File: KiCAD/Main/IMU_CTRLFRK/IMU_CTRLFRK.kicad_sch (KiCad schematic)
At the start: 9 parts, among them U3 BMM350, U7 ISM6HG256x

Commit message: Moved custom footprints into local KiCAD footprint library
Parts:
- U3: footprint BMM350:BGA9C40P3X3_128X128X50 -> LRI:BGA9C40P3X3_128X128X50
- U7: footprint ISM6HG256XTR:U_LGA-14L_2p5X3p0X0p83_STM -> LRI:ISM6
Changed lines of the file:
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@@
 			)
 		)
-		(property "Footprint" "BMM350:BGA9C40P3X3_128X128X50"
+		(property "Footprint" "LRI:BGA9C40P3X3_128X128X50"
 			(at 190.5 101.6 0)
 			(effects
@@
 			)
 		)
-		(property "Footprint" "ISM6HG256XTR:U_LGA-14L_2p5X3p0X0p83_STM"
+		(property "Footprint" "LRI:ISM6"
 			(at 127 101.6 0)
 			(effects

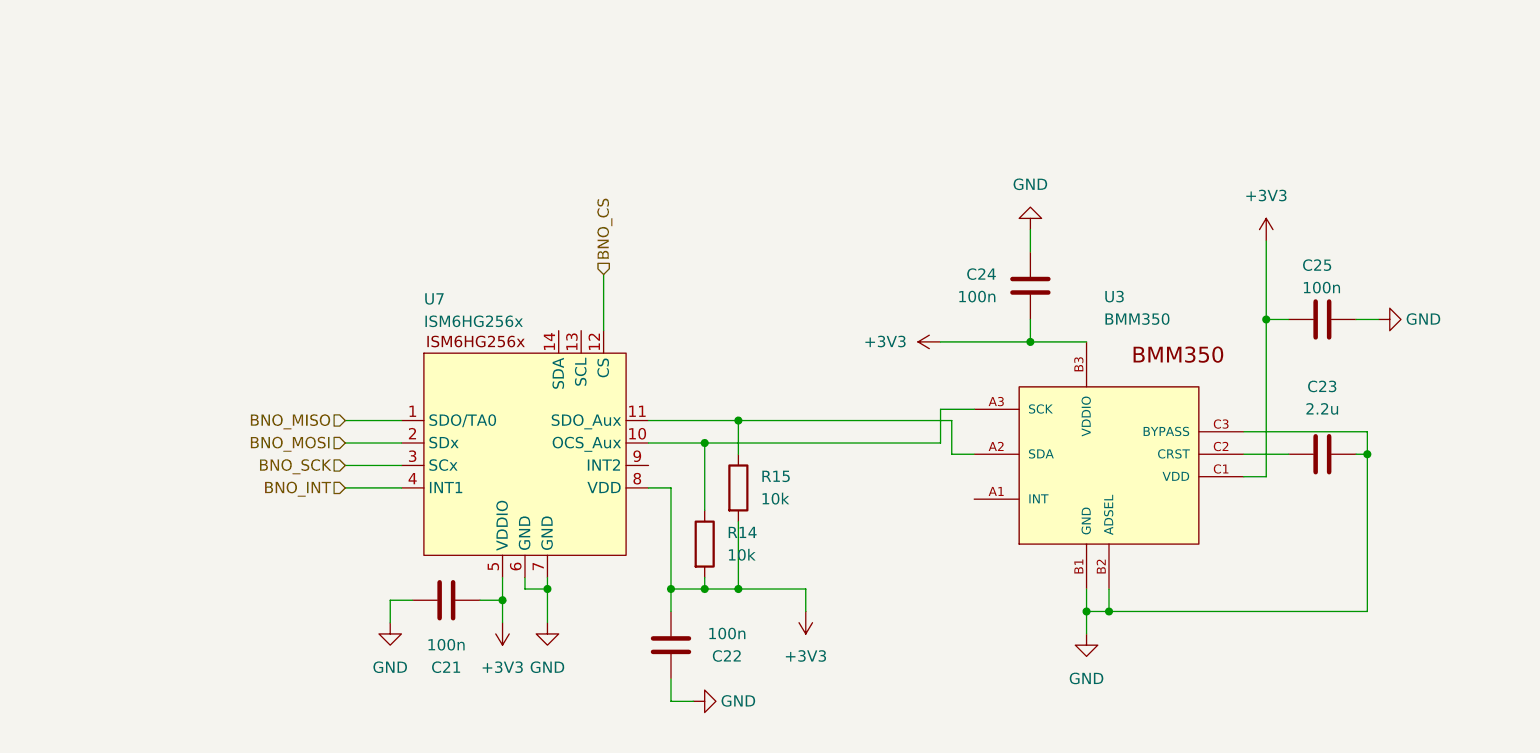
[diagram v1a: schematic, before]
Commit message: Fixed controller SCL/SDA pins
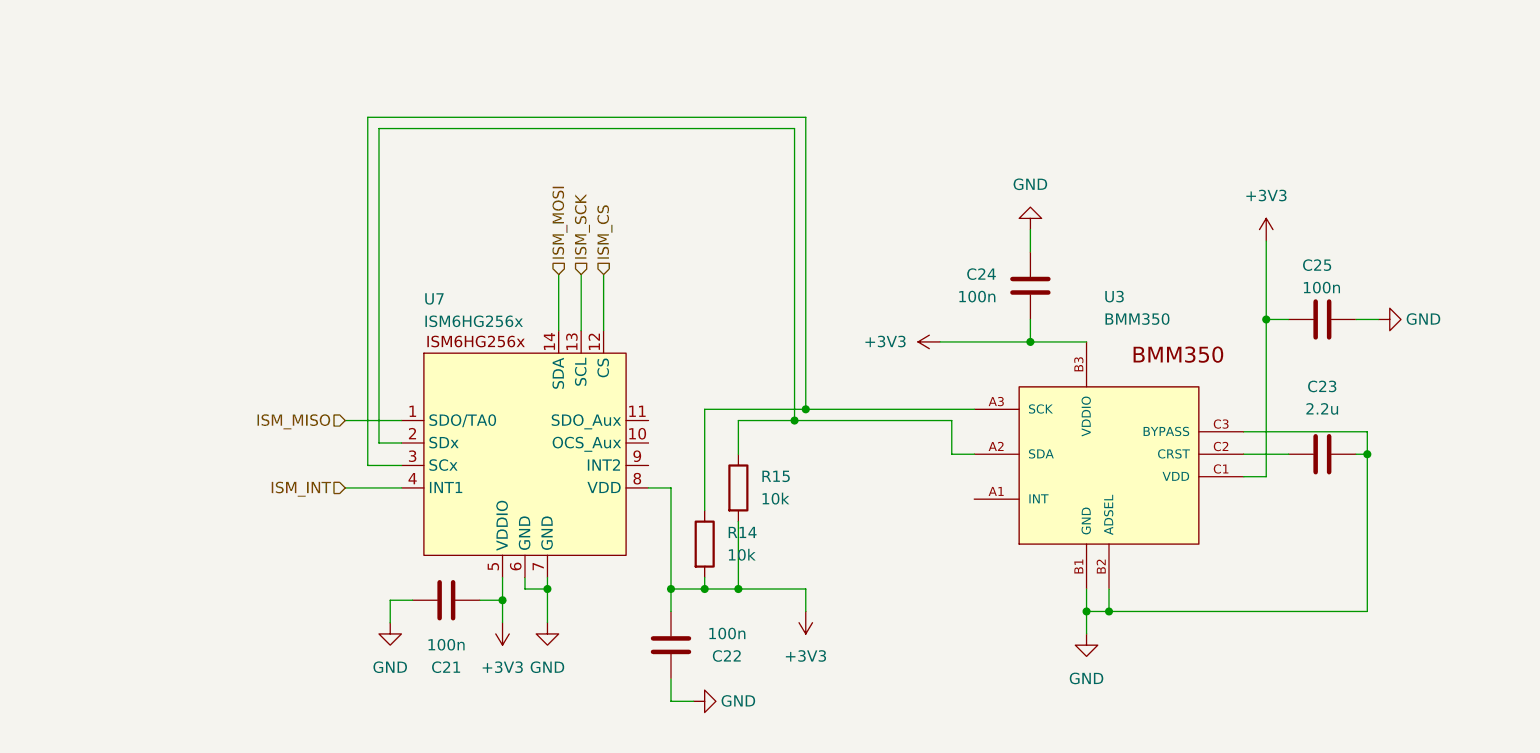
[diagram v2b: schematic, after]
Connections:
- net BNO_MOSI is gone; now on an unnamed net: U7.2 (SDx)
- net BNO_SCK is gone; now on an unnamed net: U7.3 (SCx)
- net at R15.1, U3.A2 (SDA): no longer U7.11 (SDO_Aux)
- net at R14.1, U3.A3 (SCK): no longer U7.10 (OCS_Aux)
- net ISM_SCK: now reaches U7.13 (SCL)
- net ISM_MOSI: now reaches U7.14 (SDA)
- net BNO_CS renamed ISM_CS
- net BNO_INT renamed ISM_INT
- net BNO_MISO renamed ISM_MISO
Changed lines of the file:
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@@
 	(paper "A4")
 	(junction
-		(at 147.32 100.33)
-		(diameter 0)
-		(color 0 0 0 0)
-	)
-	(junction
 		(at 147.32 116.84)
 		(diameter 0)
@@
 	)
 	(junction
+		(at 157.48 97.79)
+		(diameter 0)
+		(color 0 0 0 0)
+	)
+	(junction
 		(at 151.13 116.84)
 		(diameter 0)
@@
 	)
 	(junction
-		(at 151.13 97.79)
+		(at 158.75 96.52)
 		(diameter 0)
 		(color 0 0 0 0)
@@
 	(wire
 		(pts
-			(xy 140.97 97.79) (xy 151.13 97.79)
+			(xy 113.03 102.87) (xy 109.22 102.87)
 		)
 		(stroke
@@
 	(wire
 		(pts
+			(xy 109.22 102.87) (xy 109.22 63.5)
+		)
+		(stroke
+			(width 0)
+			(type default)
+		)
+	)
+	(wire
+		(pts
 			(xy 111.76 120.65) (xy 111.76 118.11)
 		)
@@
 	(wire
 		(pts
+			(xy 113.03 100.33) (xy 110.49 100.33)
+		)
+		(stroke
+			(width 0)
+			(type default)
+		)
+	)
+	(wire
+		(pts
 			(xy 121.92 118.11) (xy 124.46 118.11)
 		)
@@
 	(wire
 		(pts
-			(xy 173.99 96.52) (xy 173.99 100.33)
+			(xy 110.49 64.77) (xy 157.48 64.77)
+		)
+		(stroke
+			(width 0)
+			(type default)
+		)
+	)
+	(wire
+		(pts
+			(xy 133.35 81.28) (xy 133.35 87.63)
 		)
 		(stroke
@@
 	(wire
 		(pts
-			(xy 140.97 100.33) (xy 147.32 100.33)
-		)
-		(stroke
-			(width 0)
-			(type default)
-		)
-	)
-	(wire
-		(pts
 			(xy 124.46 115.57) (xy 124.46 118.11)
 		)
@@
 	(wire
 		(pts
-			(xy 173.99 96.52) (xy 177.8 96.52)
-		)
-		(stroke
-			(width 0)
-			(type default)
-		)
-	)
-	(wire
-		(pts
 			(xy 190.5 116.84) (xy 190.5 119.38)
 		)
@@
 	(wire
 		(pts
-			(xy 113.03 102.87) (xy 106.68 102.87)
-		)
-		(stroke
-			(width 0)
-			(type default)
-		)
-	)
-	(wire
-		(pts
 			(xy 143.51 116.84) (xy 143.51 105.41)
 		)
@@
 	(wire
 		(pts
+			(xy 157.48 97.79) (xy 175.26 97.79)
+		)
+		(stroke
+			(width 0)
+			(type default)
+		)
+	)
+	(wire
+		(pts
 			(xy 184.15 76.2) (xy 184.15 78.74)
 		)
@@
 	(wire
 		(pts
-			(xy 113.03 100.33) (xy 106.68 100.33)
-		)
-		(stroke
-			(width 0)
-			(type default)
-		)
-	)
-	(wire
-		(pts
-			(xy 173.99 100.33) (xy 147.32 100.33)
+			(xy 147.32 96.52) (xy 158.75 96.52)
 		)
 		(stroke
@@
 	(wire
 		(pts
+			(xy 157.48 64.77) (xy 157.48 97.79)
+		)
+		(stroke
+			(width 0)
+			(type default)
+		)
+	)
+	(wire
+		(pts
 			(xy 222.25 101.6) (xy 220.98 101.6)
 		)
@@
 	(wire
 		(pts
+			(xy 158.75 96.52) (xy 177.8 96.52)
+		)
+		(stroke
+			(width 0)
+			(type default)
+		)
+	)
+	(wire
+		(pts
 			(xy 106.68 105.41) (xy 113.03 105.41)
 		)
@@
 	(wire
 		(pts
+			(xy 109.22 63.5) (xy 158.75 63.5)
+		)
+		(stroke
+			(width 0)
+			(type default)
+		)
+	)
+	(wire
+		(pts
 			(xy 151.13 109.22) (xy 151.13 116.84)
 		)
@@
 	(wire
 		(pts
+			(xy 130.81 81.28) (xy 130.81 87.63)
+		)
+		(stroke
+			(width 0)
+			(type default)
+		)
+	)
+	(wire
+		(pts
 			(xy 208.28 101.6) (xy 213.36 101.6)
 		)
@@
 	(wire
 		(pts
-			(xy 151.13 97.79) (xy 175.26 97.79)
+			(xy 151.13 97.79) (xy 157.48 97.79)
 		)
 		(stroke
@@
 	(wire
 		(pts
-			(xy 147.32 100.33) (xy 147.32 107.95)
+			(xy 147.32 96.52) (xy 147.32 107.95)
+		)
+		(stroke
+			(width 0)
+			(type default)
+		)
+	)
+	(wire
+		(pts
+			(xy 110.49 100.33) (xy 110.49 64.77)
 		)
 		(stroke
@@
 		)
 	)
-	(hierarchical_label "BNO_SCK"
+	(wire
+		(pts
+			(xy 158.75 63.5) (xy 158.75 96.52)
+		)
+		(stroke
+			(width 0)
+			(type default)
+		)
+	)
+	(hierarchical_label "ISM_MOSI"
 		(shape input)
-		(at 106.68 102.87 180)
+		(at 130.81 81.28 90)
 		(effects
 			(font
 				(size 1.27 1.27)
 			)
-			(justify right)
-		)
-	)
-	(hierarchical_label "BNO_MISO"
+			(justify left)
+		)
+	)
+	(hierarchical_label "ISM_MISO"
 		(shape input)
 		(at 106.68 97.79 180)
@@
 		)
 	)
-	(hierarchical_label "BNO_MOSI"
+	(hierarchical_label "ISM_SCK"
 		(shape input)
-		(at 106.68 100.33 180)
+		(at 133.35 81.28 90)
 		(effects
 			(font
 				(size 1.27 1.27)
 			)
-			(justify right)
-		)
-	)
-	(hierarchical_label "BNO_CS"
+			(justify left)
+		)
+	)
+	(hierarchical_label "ISM_CS"
 		(shape input)
 		(at 135.89 81.28 90)
@@
 		)
 	)
-	(hierarchical_label "BNO_INT"
+	(hierarchical_label "ISM_INT"
 		(shape input)
 		(at 106.68 105.41 180)

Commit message: Changed BMM350 for LIS2MDL
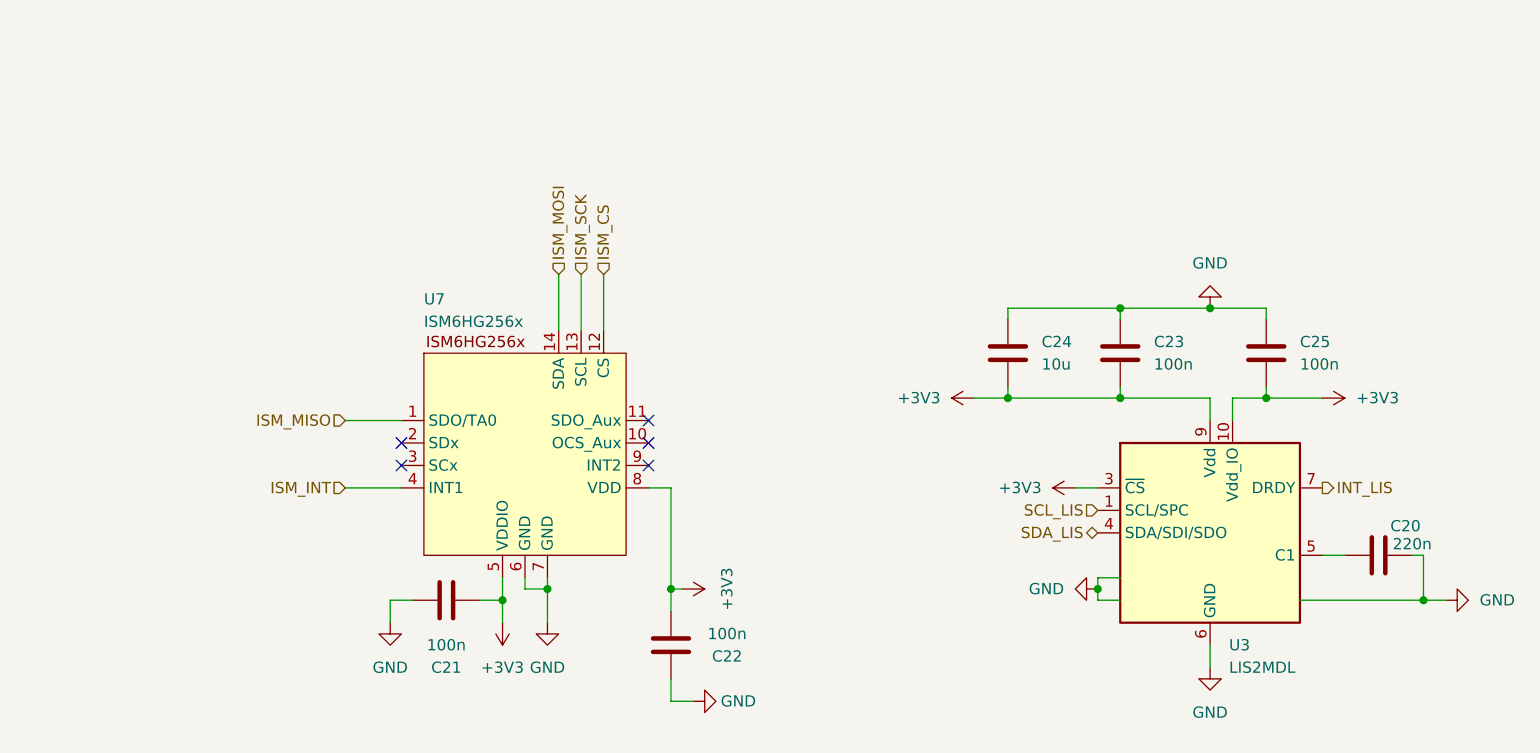
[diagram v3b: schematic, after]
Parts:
- removed R14, R15: 10k, Resistor_SMD:R_0603_1608Metric, symbol Device:R
- removed U3: BMM350, LRI:BGA9C40P3X3_128X128X50, symbol BMM350:BMM350
- added C20: 220n, Capacitor_SMD:C_0603_1608Metric, symbol Device:C
- added U3: LIS2MDL, Package_LGA:LGA-12_2x2mm_P0.5mm, symbol Sensor_Magnetic:LIS2MDL
- C23: value 2.2u -> 100n
- C24: value 100n -> 10u
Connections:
- net +3V3: now also C23.1, C24.1, C25.1, U3.10 (Vdd_IO), U3.3 (~{CS}), U3.9 (Vdd); no longer C24.2, C25.2
- net GND: now also C24.2, C25.2, C20.2, U3.11 (NC), U3.12 (NC), U3.2 (NC), U3.6 (GND), U3.8 (GND); no longer C24.1, C25.1
- new net: C20.1, U3.5 (C1)
- new net INT_LIS: U3.7 (DRDY)
- new net SCL_LIS: U3.1 (SCL/SPC)
- new net SDA_LIS: U3.4 (SDA/SDI/SDO)
- no-connect marks 0 -> 5

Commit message: Update aux magnetometer, test THs, and silkscreens
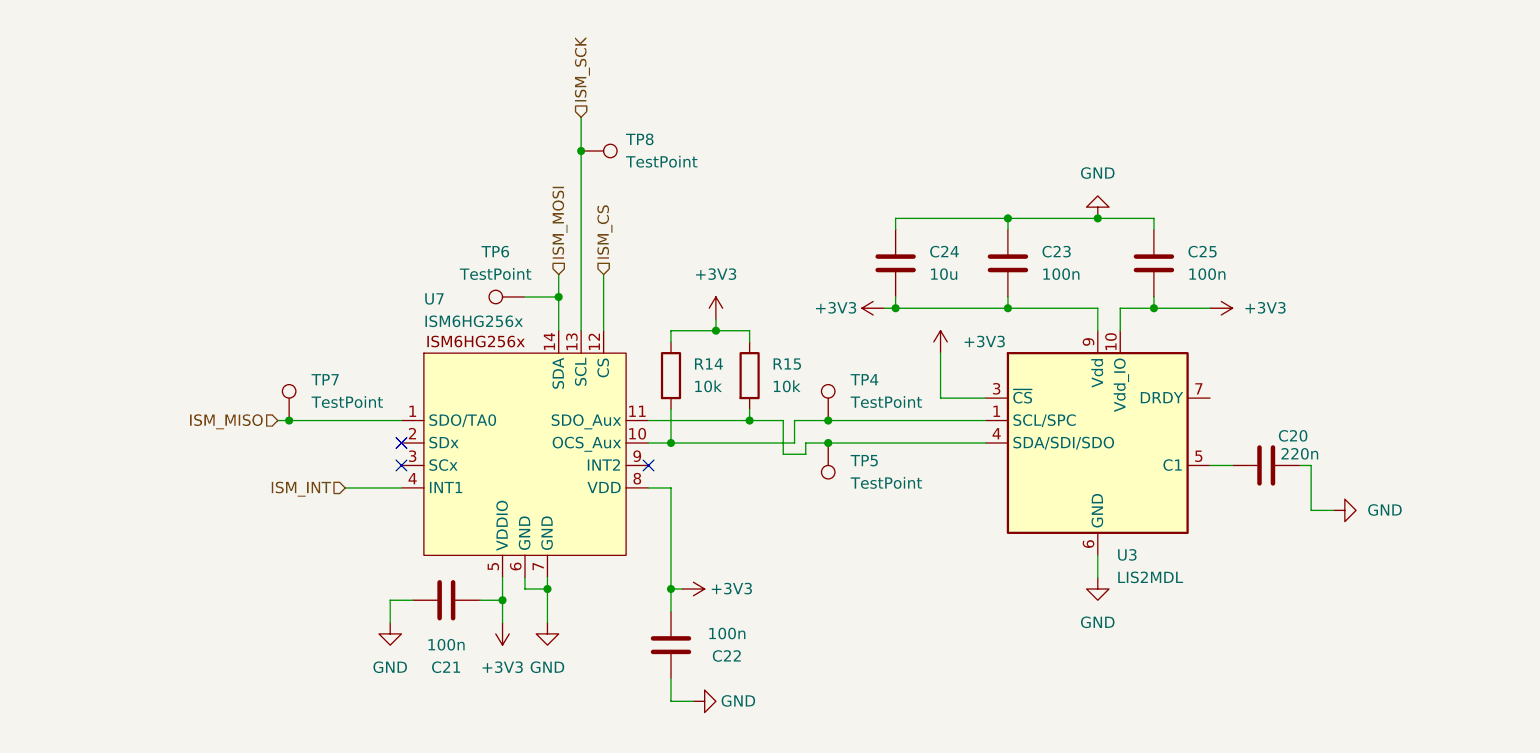
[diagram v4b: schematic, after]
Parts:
- added R14, R15: 10k, Resistor_SMD:R_0603_1608Metric, symbol Device:R
- added TP4, TP5, TP6, TP7, TP8: TestPoint, TestPoint:TestPoint_THTPad_1.5x1.5mm_Drill0.7mm, symbol Connector:TestPoint
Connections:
- net SCL_LIS is gone; now on an unnamed net: U3.1 (SCL/SPC)
- net SDA_LIS is gone; now on an unnamed net: U3.4 (SDA/SDI/SDO)
- net +3V3: now also R14.1, R15.1
- net GND: no longer U3.11 (NC), U3.12 (NC), U3.2 (NC)
- net ISM_MISO: now also TP7.1
- net ISM_MOSI: now also TP6.1
- net ISM_SCK: now also TP8.1
- net at U7.10 (OCS_Aux): now also R14.2, TP4.1
- net at U7.11 (SDO_Aux): now also R15.2, TP5.1
- net INT_LIS: no longer names the net of U3.7 (DRDY)
- no-connect marks 5 -> 3
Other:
- moved on the sheet: C20, C23, C24, C25

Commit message: Replace independent magnetometer, reformat test points, generate test gerber and BOM
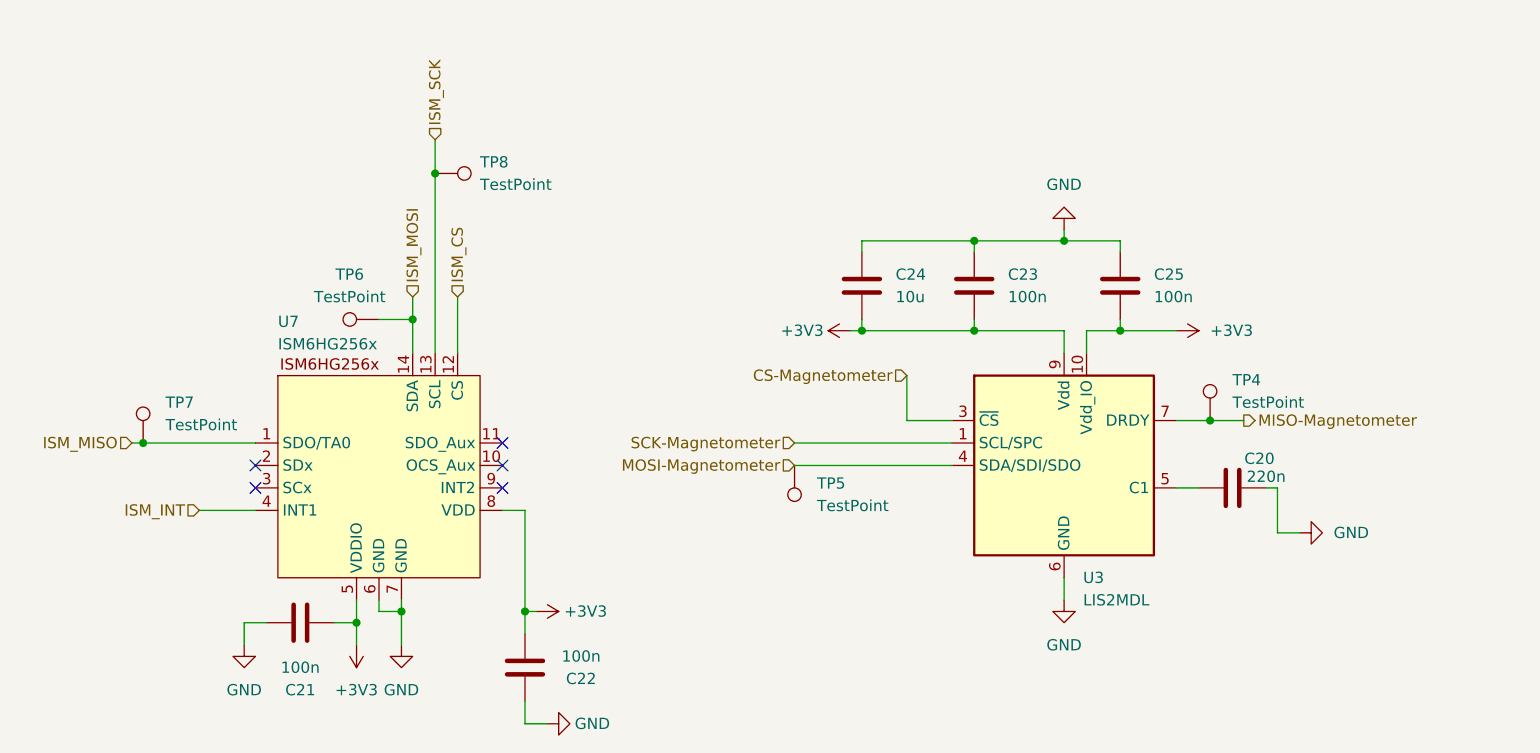
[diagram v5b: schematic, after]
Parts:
- removed R14, R15: 10k, Resistor_SMD:R_0603_1608Metric, symbol Device:R
- TP4, TP5, TP6, TP7, TP8: footprint TestPoint:TestPoint_THTPad_1.5x1.5mm_Drill0.7mm -> TestPoint:TestPoint_Pad_D1.0mm
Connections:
- net +3V3: no longer U3.3 (~{CS})
- net MOSI-Magnetometer: now reaches TP5.1, U3.4 (SDA/SDI/SDO)
- net MOSI-Magnetometer: no longer U7.11 (SDO_Aux)
- net MISO-Magnetometer: now reaches U3.7 (DRDY)
- net MISO-Magnetometer: now also TP4.1
- new net CS-Magnetometer: U3.3 (~{CS})
- new net SCK-Magnetometer: U3.1 (SCL/SPC)
- now unconnected: U7.10 (OCS_Aux)
- no-connect marks 3 -> 5
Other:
- moved on the sheet: C20, C21, C22, C23, C24, C25, TP4, TP5, TP6, TP7, TP8, U3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

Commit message: Update BOM and respective components according to LCSC supply, remove previously generated production files
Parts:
- TP4, TP5, TP6, TP7, TP8: now left out of the parts list
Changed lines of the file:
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@@
 		(unit 1)
 		(exclude_from_sim no)
-		(in_bom yes)
+		(in_bom no)
 		(on_board yes)
 		(dnp no)
@@
 		(unit 1)
 		(exclude_from_sim no)
-		(in_bom yes)
+		(in_bom no)
 		(on_board yes)
 		(dnp no)
@@
 		(unit 1)
 		(exclude_from_sim no)
-		(in_bom yes)
+		(in_bom no)
 		(on_board yes)
 		(dnp no)
@@
 		(unit 1)
 		(exclude_from_sim no)
-		(in_bom yes)
+		(in_bom no)
 		(on_board yes)
 		(dnp no)
@@
 		(unit 1)
 		(exclude_from_sim no)
-		(in_bom yes)
-		(on_board yes)
-		(dnp no)
+		(in_bom no)
+		(on_board yes)
+		(dnp no)

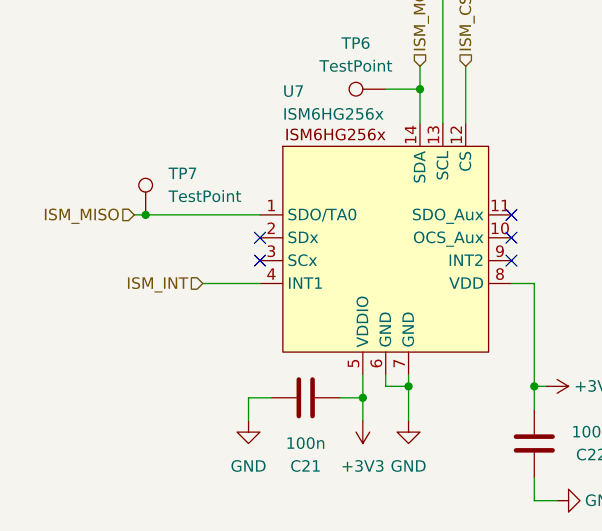
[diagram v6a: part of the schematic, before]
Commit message: save after realizing branch was not switched to layoutv2
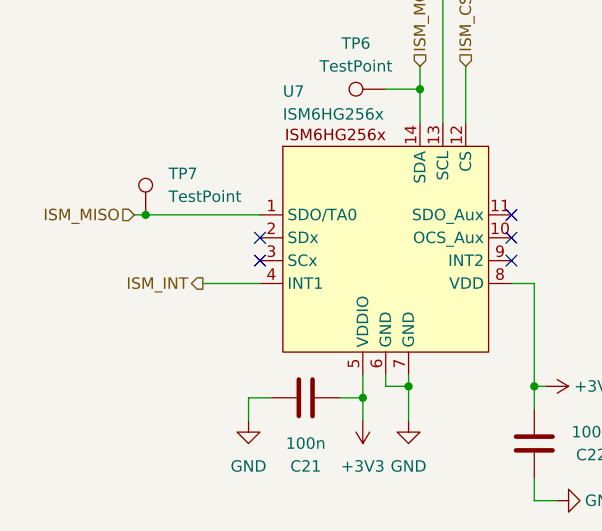
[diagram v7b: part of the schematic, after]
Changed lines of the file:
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@@
 	)
 	(hierarchical_label "ISM_INT"
-		(shape input)
+		(shape output)
 		(at 90.17 107.95 180)
 		(effects
